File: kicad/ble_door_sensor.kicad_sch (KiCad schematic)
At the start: 40 parts, among them J1 Prog Header, J101 Conn_01x08, Q1 ALS-PT19, SW101 SW_Reed, SW102 SW_Push, T1 ToolingHole, T2 ToolingHole, T3 ToolingHole, U1 nRF52832-QFxx, U101 TMP100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

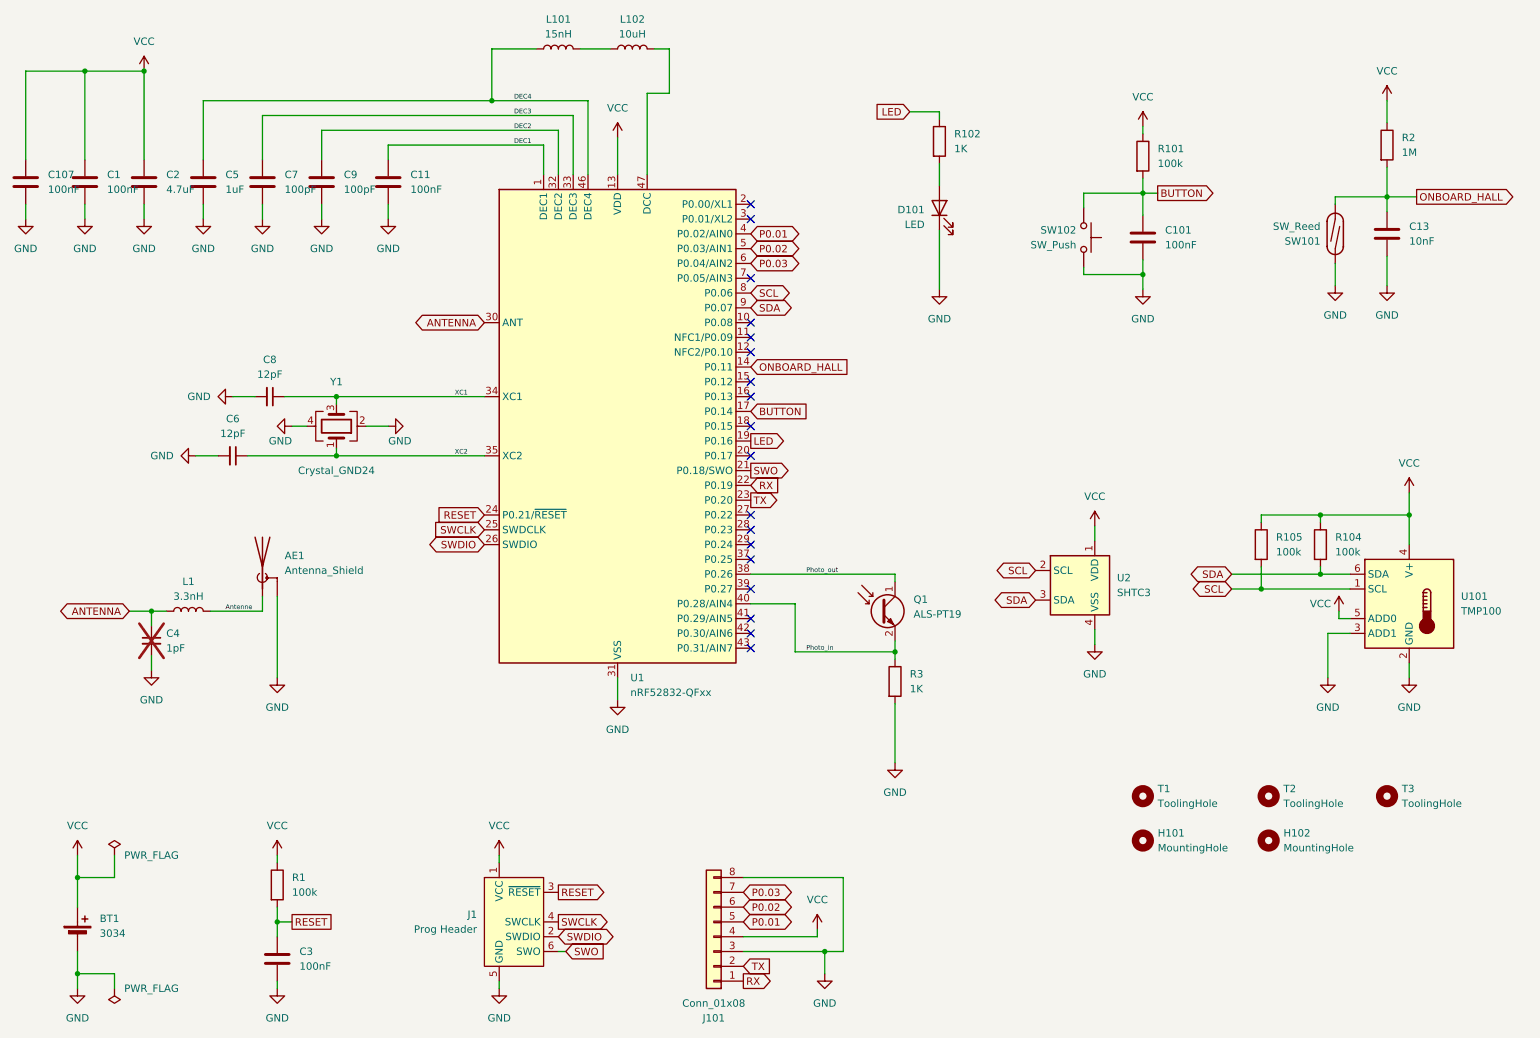
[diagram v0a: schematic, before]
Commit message: Update to Kicad 8
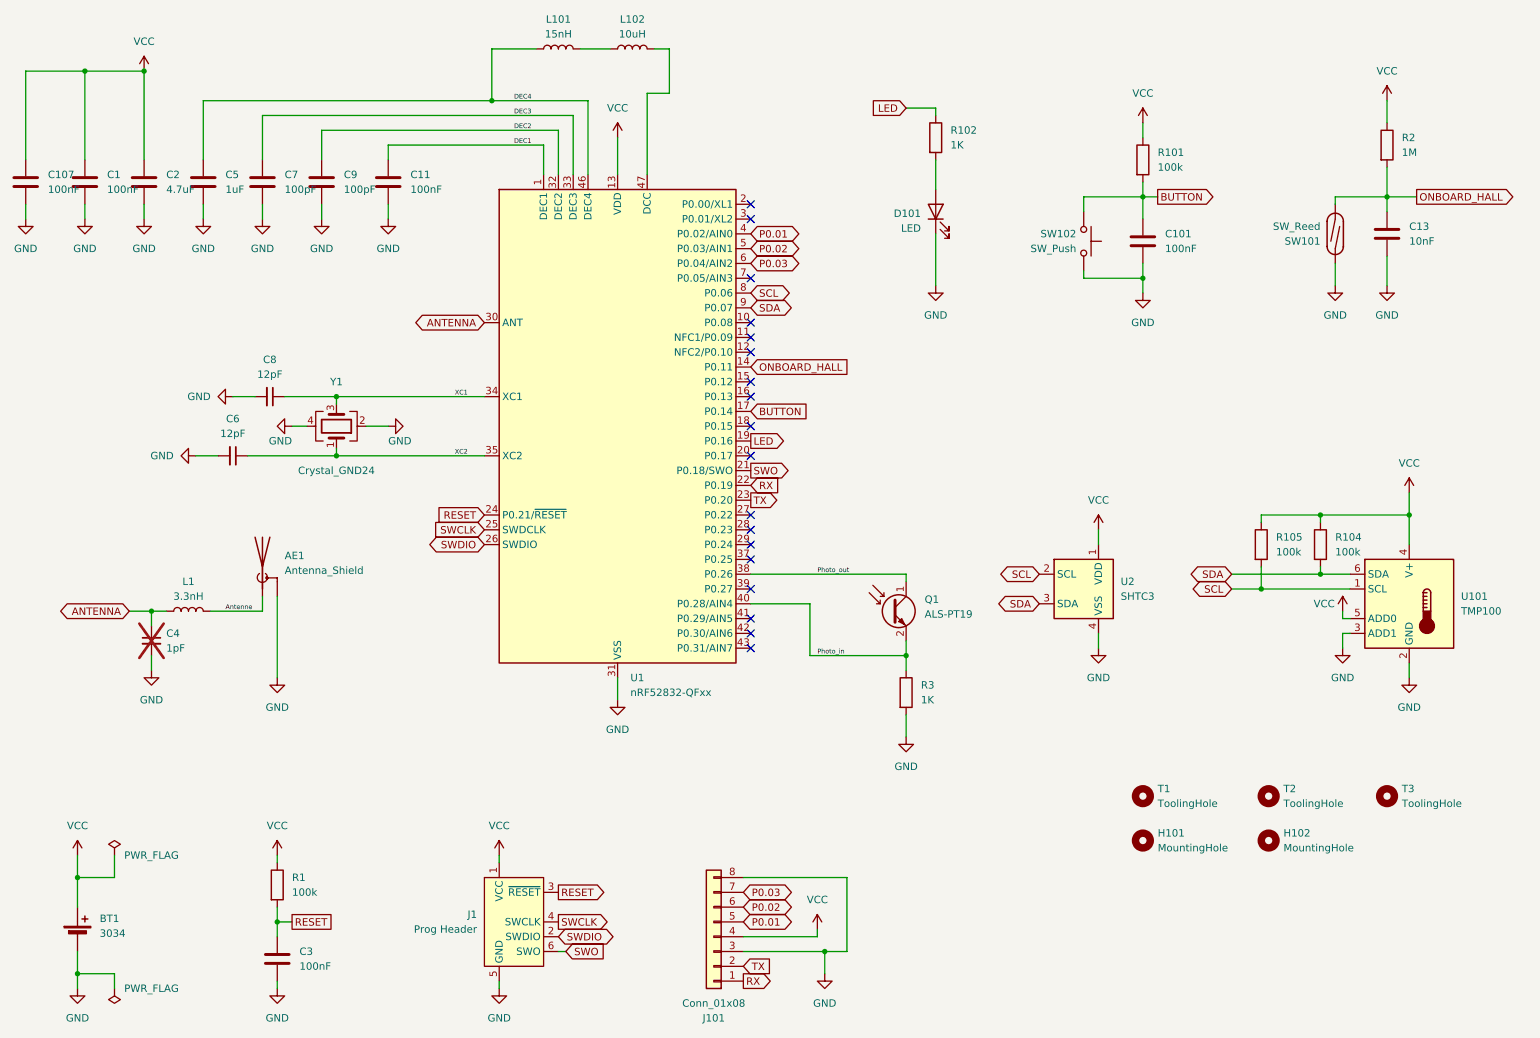
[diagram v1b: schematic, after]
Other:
- moved on the sheet: C101, D101, Q1, R101, R102, R3, SW102, U2

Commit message: Move footprints to new library
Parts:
- SW101: footprint Library:reed_contact -> g-Sensors:reed_contact
- T1, T2, T3: footprint Library:JLCPCB_Mounting_hole -> g-Misc:JLCPCB_Mounting_hole
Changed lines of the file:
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@@
 			)
 		)
-		(property "Footprint" "Library:JLCPCB_Mounting_hole"
+		(property "Footprint" "g-Misc:JLCPCB_Mounting_hole"
 			(at 237.49 151.13 0)
 			(effects
@@
 			)
 		)
-		(property "Footprint" "Library:reed_contact"
+		(property "Footprint" "g-Sensors:reed_contact"
 			(at 248.92 54.61 0)
 			(effects
@@
 			)
 		)
-		(property "Footprint" "Library:JLCPCB_Mounting_hole"
+		(property "Footprint" "g-Misc:JLCPCB_Mounting_hole"
 			(at 257.81 151.13 0)
 			(effects
@@
 			)
 		)
-		(property "Footprint" "Library:JLCPCB_Mounting_hole"
+		(property "Footprint" "g-Misc:JLCPCB_Mounting_hole"
 			(at 215.9 151.13 0)
 			(effects

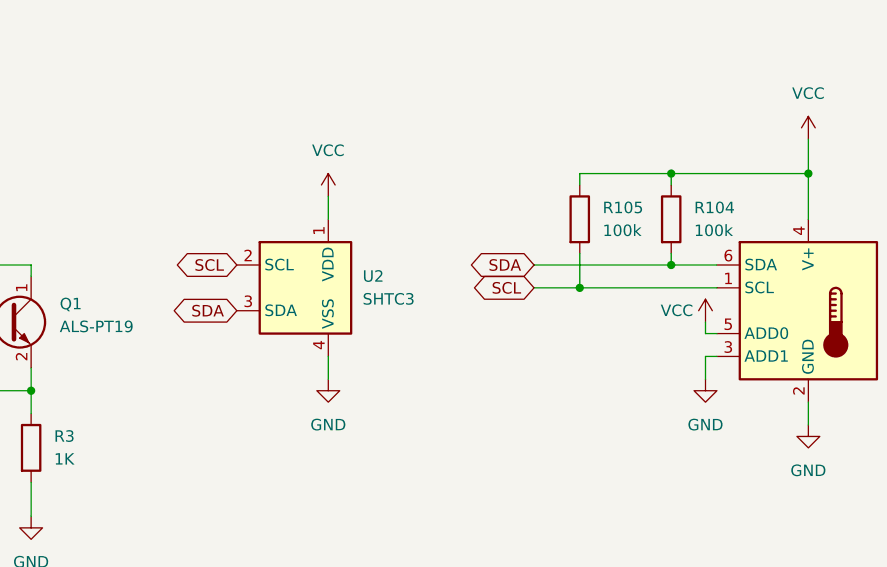
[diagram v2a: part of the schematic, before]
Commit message: Added hints about i"c addresses
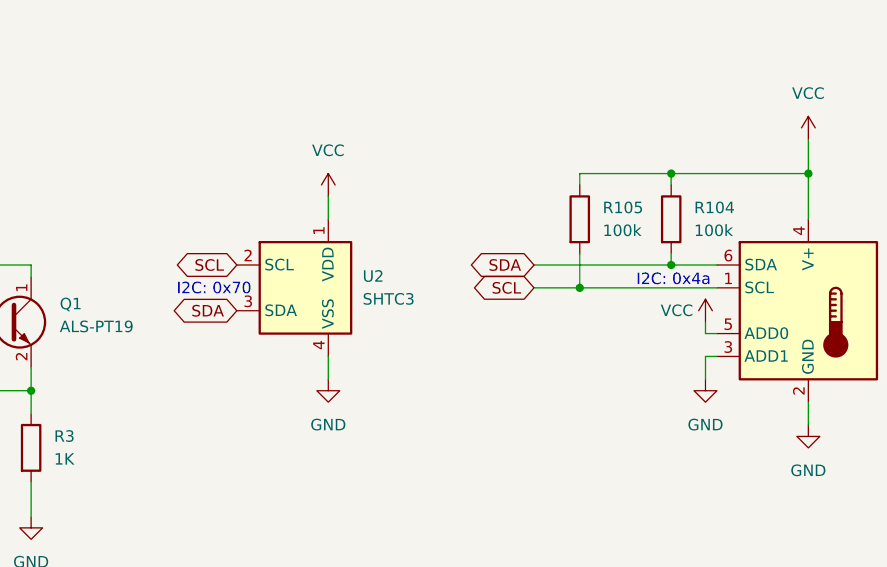
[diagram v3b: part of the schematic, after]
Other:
- note added: "I2C: 0x4a"
- note added: "I2C: 0x70"
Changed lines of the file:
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@@
+		)
+	)
+	(text "I2C: 0x4a"
+		(exclude_from_sim no)
+		(at 246.634 114.808 0)
+		(effects
+			(font
+				(size 1.27 1.27)
+			)
+		)
+	)
+	(text "I2C: 0x70"
+		(exclude_from_sim no)
+		(at 195.58 115.824 0)
+		(effects
+			(font
+				(size 1.27 1.27)
+			)
 		)
 	)

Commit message: Update to kicad 9
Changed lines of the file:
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@@
 (kicad_sch
-	(version 20231120)
+	(version 20250114)
 	(generator "eeschema")
-	(generator_version "8.0")
+	(generator_version "9.0")
 	(paper "A4")
 	(title_block
@@
 		(company "Fabian Pflug")
 	)
+	(text "I2C: 0x4a"
+		(exclude_from_sim no)
+		(at 246.634 114.808 0)
+		(effects
+			(font
+				(size 1.27 1.27)
+			)
+		)
+	)
+	(text "I2C: 0x70"
+		(exclude_from_sim no)
+		(at 195.58 115.824 0)
+		(effects
+			(font
+				(size 1.27 1.27)
+			)
+		)
+	)
 	(junction
 		(at 215.9 48.26)
@@
 		)
 	)
-	(text "I2C: 0x4a"
-		(exclude_from_sim no)
-		(at 246.634 114.808 0)
-		(effects
-			(font
-				(size 1.27 1.27)
-			)
-		)
-	)
-	(text "I2C: 0x70"
-		(exclude_from_sim no)
-		(at 195.58 115.824 0)
-		(effects
-			(font
-				(size 1.27 1.27)
-			)
-		)
-	)
 	(label "DEC3"
 		(at 107.95 34.29 0)
-		(fields_autoplaced yes)
 		(effects
 			(font
@@
 	(label "XC2"
 		(at 97.79 92.71 0)
-		(fields_autoplaced yes)
 		(effects
 			(font
@@
 	(label "XC1"
 		(at 97.79 82.55 0)
-		(fields_autoplaced yes)
 		(effects
 			(font
@@
 	(label "DEC4"
 		(at 107.95 31.75 0)
-		(fields_autoplaced yes)
 		(effects
 			(font
@@
 	(label "DEC1"
 		(at 107.95 39.37 0)
-		(fields_autoplaced yes)
 		(effects
 			(font
@@
 	(label "Antenne"
 		(at 58.42 119.38 0)
-		(fields_autoplaced yes)
 		(effects
 			(font
@@
 	(label "Photo_in"
 		(at 160.02 127 0)
-		(fields_autoplaced yes)
 		(effects
 			(font
@@
 	(label "Photo_out"
 		(at 160.02 113.03 0)
-		(fields_autoplaced yes)
 		(effects
 			(font
@@
 	(label "DEC2"
 		(at 107.95 36.83 0)
-		(fields_autoplaced yes)
 		(effects
 			(font
@@
 		)
 	)
+	(embedded_fonts no)
 )

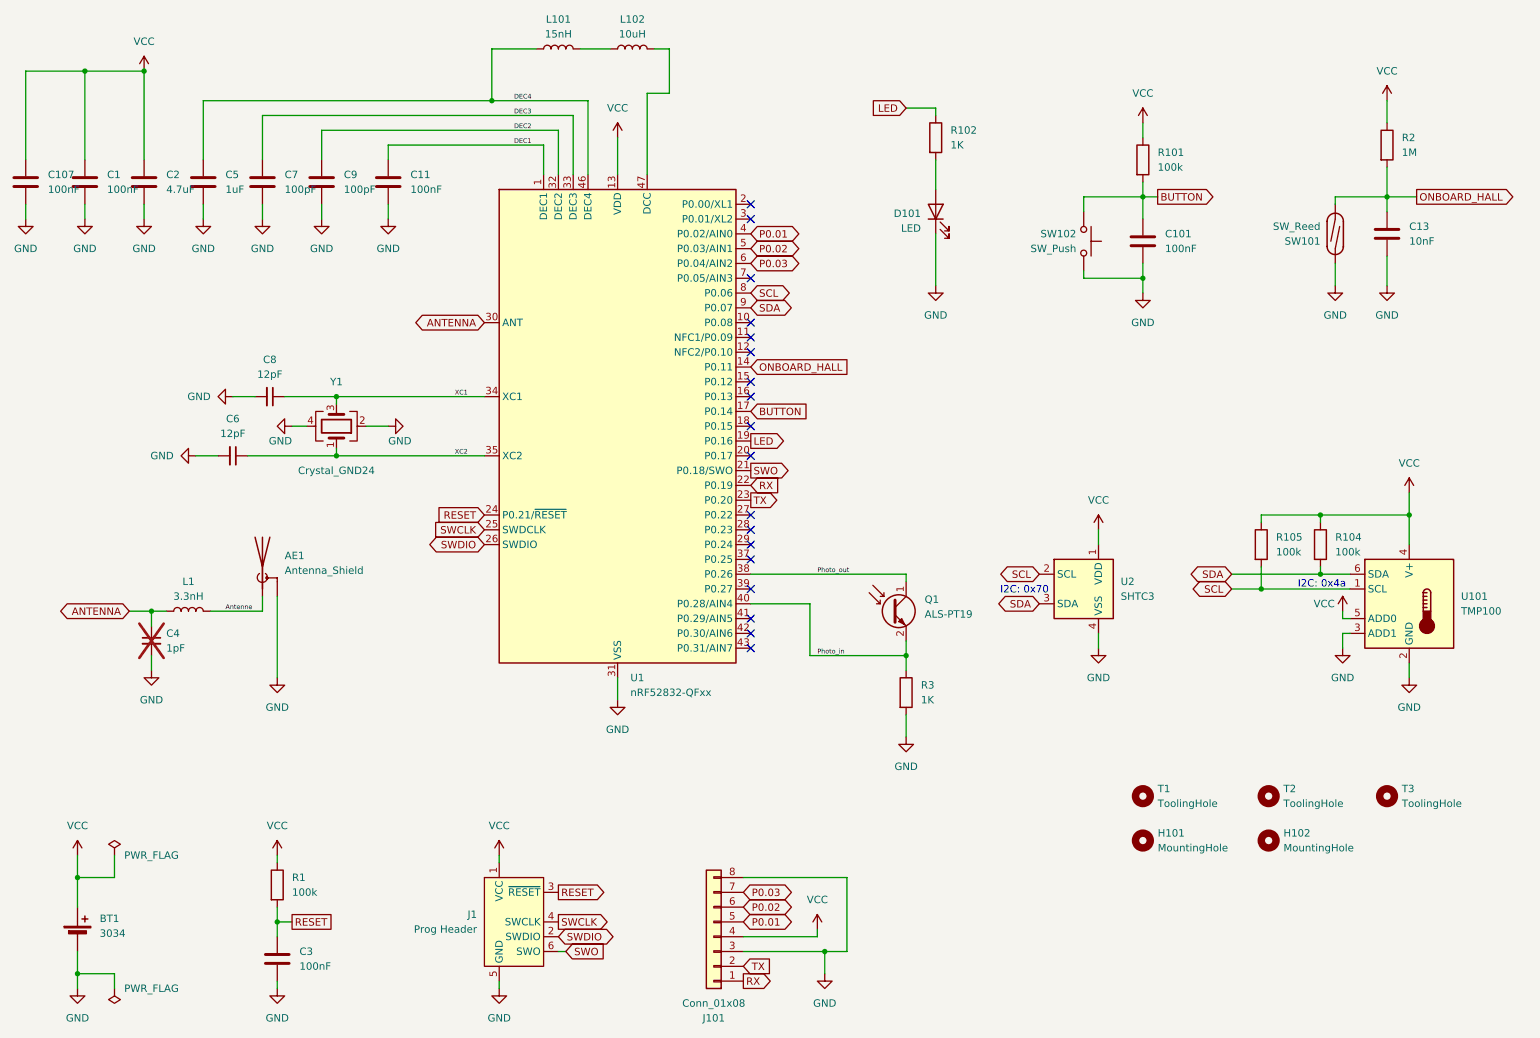
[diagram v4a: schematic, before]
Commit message: Move all sensors to their own sheet
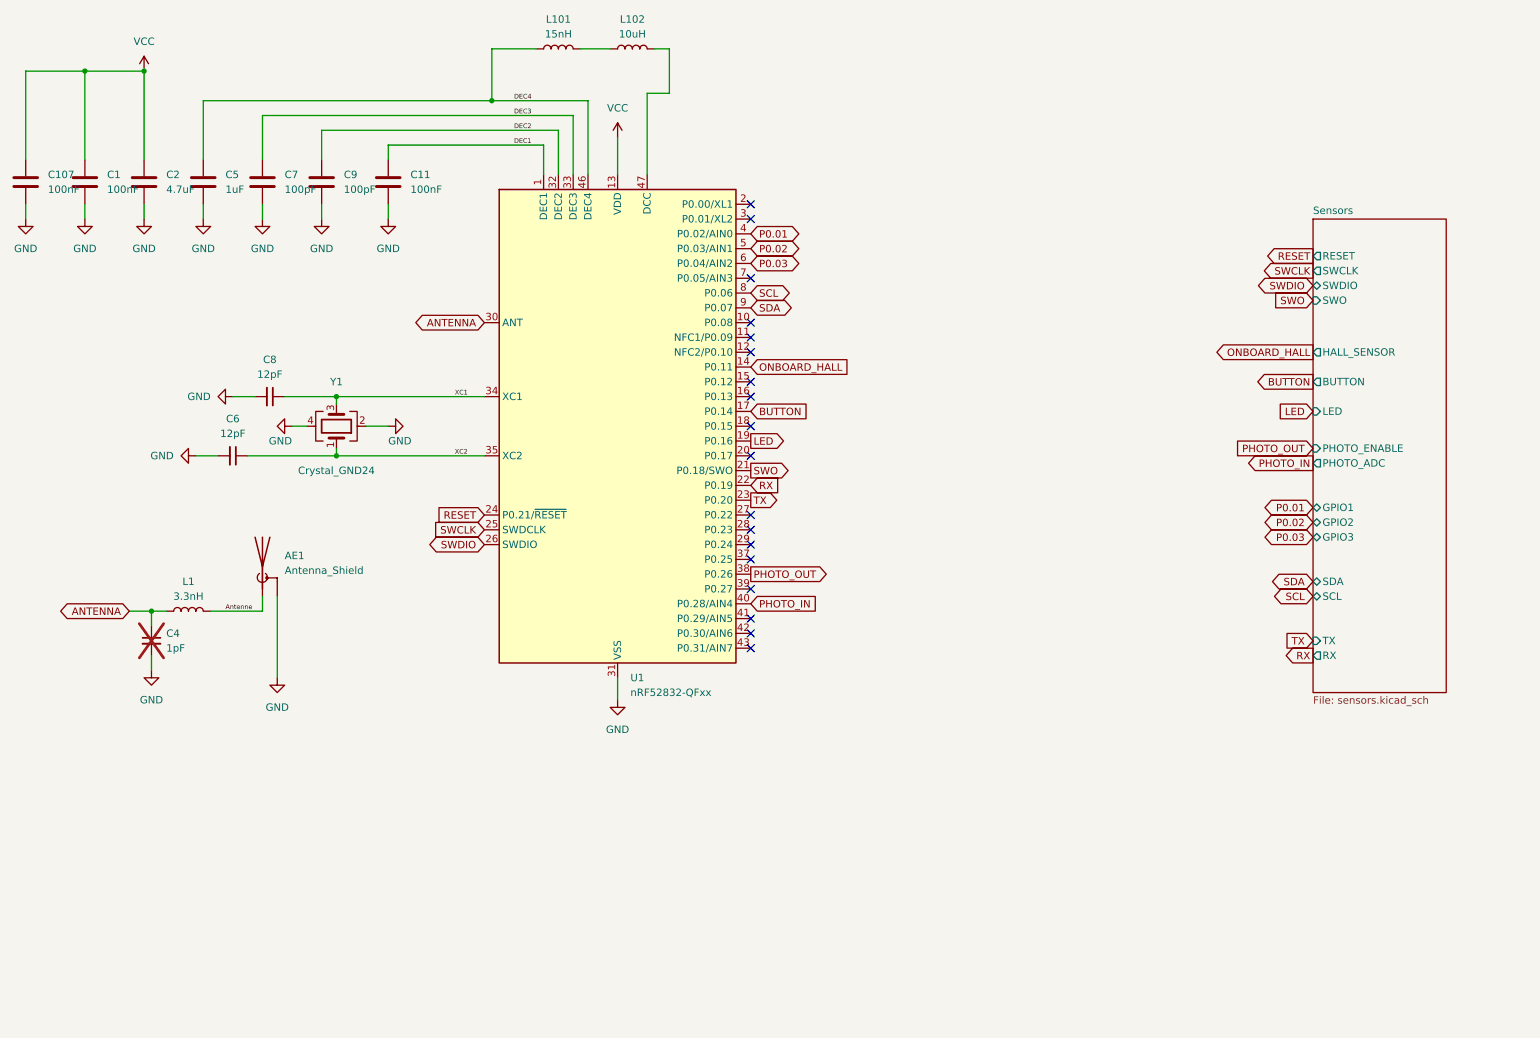
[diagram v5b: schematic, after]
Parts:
- removed BT1: 3034, Battery:BatteryHolder_Keystone_3034_1x20mm, symbol Device:Battery_Cell
- removed C101, C3: 100nF, Capacitor_SMD:C_0402_1005Metric, symbol Device:C
- removed C13: 10nF, Capacitor_SMD:C_0402_1005Metric, symbol Device:C
- removed D101: LED, LED_SMD:LED_0603_1608Metric, symbol Device:LED
- removed H101, H102: MountingHole, MountingHole:MountingHole_2.2mm_M2, symbol Mechanical:MountingHole
- removed J1: Prog Header, Connector:Tag-Connect_TC2030-IDC-NL_2x03_P1.27mm_Vertical, symbol Connector:Conn_ARM_SWD_TagConnect_TC2030-NL
- removed J101: Conn_01x08, Connector_PinHeader_2.54mm:PinHeader_1x08_P2.54mm_Vertical_SMD_Pin1Left, symbol Connector_Generic:Conn_01x08
- removed Q1: ALS-PT19, LED_SMD:LED_0603_1608Metric, symbol Device:Q_Photo_NPN
- removed R1, R101, R104, R105: 100k, Resistor_SMD:R_0402_1005Metric, symbol Device:R
- removed R102, R3: 1K, Resistor_SMD:R_0402_1005Metric, symbol Device:R
- removed R2: 1M, Resistor_SMD:R_0402_1005Metric, symbol Device:R
- removed SW101: SW_Reed, g-Sensors:reed_contact, symbol Switch:SW_Reed
- removed SW102: SW_Push, Button_Switch_SMD:SW_SPST_TL3342, symbol Switch:SW_Push
- removed T1, T2, T3: ToolingHole, g-Misc:JLCPCB_Mounting_hole, symbol Mechanical:MountingHole
- removed U101: TMP100, Package_TO_SOT_SMD:SOT-23-6, symbol Sensor_Temperature:TMP100
- removed U2: SHTC3, Sensor_Humidity:Sensirion_DFN-4-1EP_2x2mm_P1mm_EP0.7x1.6mm, symbol Sensor_Humidity:SHTC3
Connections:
- net Photo_in renamed PHOTO_IN
- net Photo_out renamed PHOTO_OUT
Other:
- added sheet Sensors (sensors.kicad_sch)
- note removed: "I2C: 0x4a"
- note removed: "I2C: 0x70"
